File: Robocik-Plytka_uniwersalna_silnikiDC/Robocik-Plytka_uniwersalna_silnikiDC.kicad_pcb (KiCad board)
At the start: 2 copper layers, 49.6 x 66.8 mm, 67 parts, among them IC1 ACSL-6400-00TE, IC2 L6205D, J1 Conn_01x03, J2 Conn_01x02, J3 Conn_01x04, J4 Conn_01x02, J5 Conn_01x03, J6 Conn_01x02, Q1 BC847, Q2 BC847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

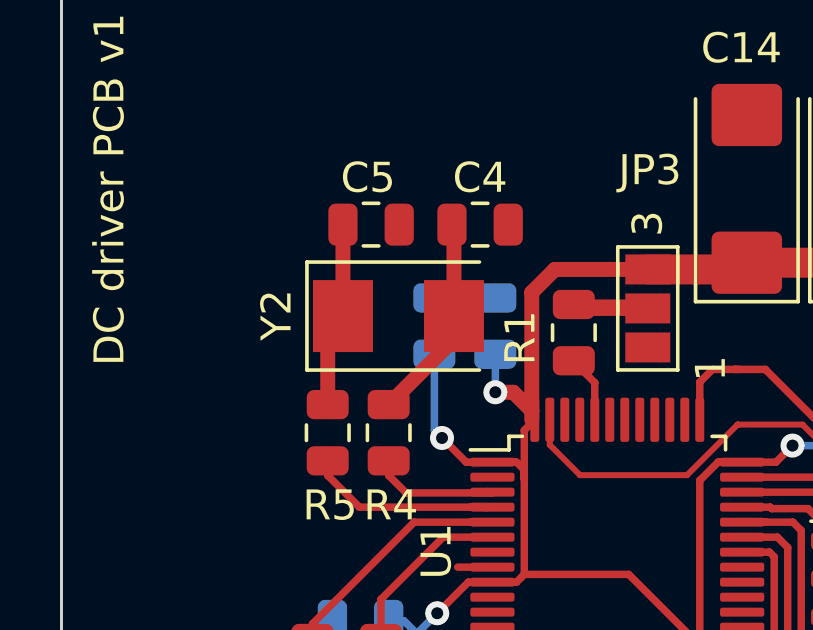
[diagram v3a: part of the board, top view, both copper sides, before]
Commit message: Fixed size of LSE crystal oscilator. Added 3D models for LSE and HSE oscilators.
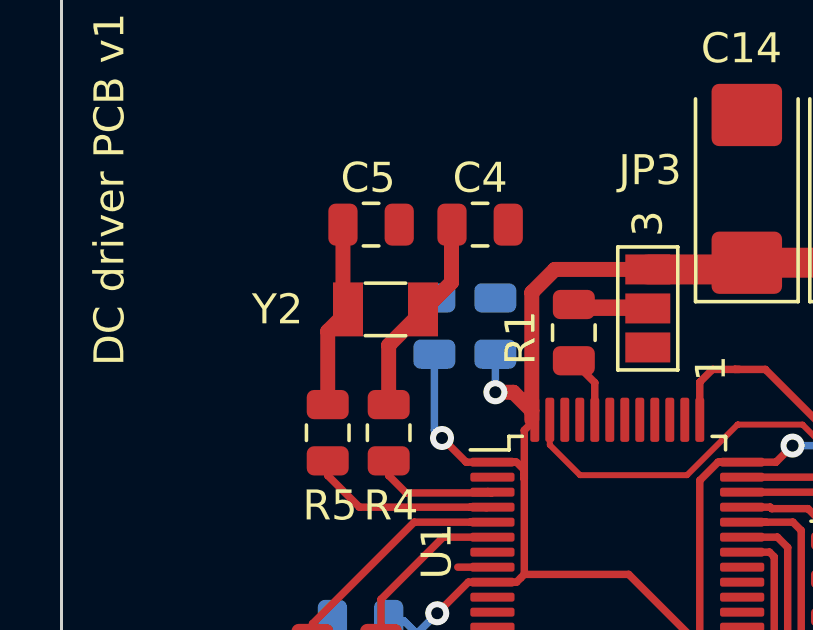
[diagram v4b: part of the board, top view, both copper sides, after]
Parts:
- Y2: footprint Crystal:Crystal_SMD_5032-2Pin_5.0x3.2mm -> Crystal:Crystal_SMD_3215-2Pin_3.2x1.5mm
- moved Y2 0.49 mm to (135.2, 81.6), turned to 180 degrees
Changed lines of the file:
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@@
     (thickness 1.6)
     (drawings 13)
-    (tracks 472)
+    (tracks 473)
     (zones 0)
     (modules 67)
@@
   )
   (setup
-    (last_trace_width 0.25)
+    (last_trace_width 0.5)
     (user_trace_width 0.2)
     (user_trace_width 0.5)
@@
     (add_net VddPWR)
   )
+  (module Crystal:Crystal_SMD_3215-2Pin_3.2x1.5mm (layer F.Cu)
+    (at 135.2 81.6 180)
+    (descr "SMD Crystal FC-135 https://support.epson.biz/td/api/doc_check.php?dl=brief_FC-135R_en.pdf")
+    (tags "SMD SMT Crystal")
+    (attr smd)
+    (fp_text reference Y2 (at 3.6 0 180) (layer F.SilkS)
+      (effects (font (size 1 1) (thickness 0.15)))
+    )
+    (fp_text value "LSE OSC" (at 0 2 180) (layer F.Fab)
+      (effects (font (size 1 1) (thickness 0.15)))
+    )
+    (fp_line (start 2 -1.15) (end 2 1.15) (layer F.CrtYd) (width 0.05))
+    (fp_line (start -2 -1.15) (end -2 1.15) (layer F.CrtYd) (width 0.05))
+    (fp_line (start -2 1.15) (end 2 1.15) (layer F.CrtYd) (width 0.05))
+    (fp_line (start -1.6 0.75) (end 1.6 0.75) (layer F.Fab) (width 0.1))
+    (fp_line (start -1.6 -0.75) (end 1.6 -0.75) (layer F.Fab) (width 0.1))
+    (fp_line (start 1.6 -0.75) (end 1.6 0.75) (layer F.Fab) (width 0.1))
+    (fp_line (start -0.675 -0.875) (end 0.675 -0.875) (layer F.SilkS) (width 0.12))
+    (fp_line (start -0.675 0.875) (end 0.675 0.875) (layer F.SilkS) (width 0.12))
+    (fp_line (start -1.6 -0.75) (end -1.6 0.75) (layer F.Fab) (width 0.1))
+    (fp_line (start -2 -1.15) (end 2 -1.15) (layer F.CrtYd) (width 0.05))
+    (fp_text user %R (at 0 -2 180) (layer F.Fab)
+      (effects (font (size 1 1) (thickness 0.15)))
+    )
+    (pad 2 smd rect (at -1.25 0 180) (size 1 1.8) (layers F.Cu F.Paste F.Mask)
+      (net 5 "Net-(C4-Pad2)"))
+    (pad 1 smd rect (at 1.25 0 180) (size 1 1.8) (layers F.Cu F.Paste F.Mask)
+      (net 6 "Net-(C5-Pad2)"))
+    (model ${KISYS3DMOD}/Crystal.3dshapes/Crystal_SMD_3215-2Pin_3.2x1.5mm.wrl
+      (at (xyz 0 0 0))
+      (scale (xyz 1 1 1))
+      (rotate (xyz 0 0 0))
+    )
+    (model "${KIPRJMOD}/3D models/Crystal_SMD-3,2x1,5.STEP"
+      (at (xyz 0 0 0))
+      (scale (xyz 1 1 1))
+      (rotate (xyz -90 0 90))
+    )
+  )
   (module Connector_JST:JST_PH_S3B-PH-K_1x03_P2.00mm_Horizontal (layer B.Cu)
     (at 167 101.1 270)
@@
   )
   (module Crystal:Crystal_SMD_5032-2Pin_5.0x3.2mm (layer F.Cu)
-    (at 135.632 81.822)
-    (descr "SMD Crystal SERIES SMD2520/2 http://www.icbase.com/File/PDF/HKC/HKC00061008.pdf, 5.0x3.2mm^2 package")
-    (tags "SMD SMT crystal")
-    (attr smd)
-    (fp_text reference Y2 (at -4.06 -0.034 90) (layer F.SilkS)
-      (effects (font (size 1 1) (thickness 0.15)))
-    )
-    (fp_text value "LSE OSC" (at 0 2.8) (layer F.Fab)
-      (effects (font (size 1 1) (thickness 0.15)))
-    )
-    (fp_circle (center 0 0) (end 0.093333 0) (layer F.Adhes) (width 0.186667))
-    (fp_circle (center 0 0) (end 0.213333 0) (layer F.Adhes) (width 0.133333))
-    (fp_circle (center 0 0) (end 0.333333 0) (layer F.Adhes) (width 0.133333))
-    (fp_circle (center 0 0) (end 0.4 0) (layer F.Adhes) (width 0.1))
-    (fp_line (start 3.1 -1.9) (end -3.1 -1.9) (layer F.CrtYd) (width 0.05))
-    (fp_line (start 3.1 1.9) (end 3.1 -1.9) (layer F.CrtYd) (width 0.05))
-    (fp_line (start -3.1 1.9) (end 3.1 1.9) (layer F.CrtYd) (width 0.05))
-    (fp_line (start -3.1 -1.9) (end -3.1 1.9) (layer F.CrtYd) (width 0.05))
-    (fp_line (start -3.05 1.8) (end 2.7 1.8) (layer F.SilkS) (width 0.12))
-    (fp_line (start -3.05 -1.8) (end -3.05 1.8) (layer F.SilkS) (width 0.12))
-    (fp_line (start 2.7 -1.8) (end -3.05 -1.8) (layer F.SilkS) (width 0.12))
-    (fp_line (start -2.5 0.6) (end -1.5 1.6) (layer F.Fab) (width 0.1))
-    (fp_line (start -2.5 -1.4) (end -2.3 -1.6) (layer F.Fab) (width 0.1))
-    (fp_line (start -2.5 1.4) (end -2.5 -1.4) (layer F.Fab) (width 0.1))
-    (fp_line (start -2.3 1.6) (end -2.5 1.4) (layer F.Fab) (width 0.1))
-    (fp_line (start 2.3 1.6) (end -2.3 1.6) (layer F.Fab) (width 0.1))
-    (fp_line (start 2.5 1.4) (end 2.3 1.6) (layer F.Fab) (width 0.1))
-    (fp_line (start 2.5 -1.4) (end 2.5 1.4) (layer F.Fab) (width 0.1))
-    (fp_line (start 2.3 -1.6) (end 2.5 -1.4) (layer F.Fab) (width 0.1))
-    (fp_line (start -2.3 -1.6) (end 2.3 -1.6) (layer F.Fab) (width 0.1))
-    (fp_text user %R (at 0 0) (layer F.Fab)
-      (effects (font (size 1 1) (thickness 0.15)))
-    )
-    (pad 2 smd rect (at 1.85 0) (size 2 2.4) (layers F.Cu F.Paste F.Mask)
-      (net 5 "Net-(C4-Pad2)"))
-    (pad 1 smd rect (at -1.85 0) (size 2 2.4) (layers F.Cu F.Paste F.Mask)
-      (net 6 "Net-(C5-Pad2)"))
-    (model ${KISYS3DMOD}/Crystal.3dshapes/Crystal_SMD_5032-2Pin_5.0x3.2mm.wrl
-      (at (xyz 0 0 0))
-      (scale (xyz 1 1 1))
-      (rotate (xyz 0 0 0))
-    )
-  )
-  (module Crystal:Crystal_SMD_5032-2Pin_5.0x3.2mm (layer F.Cu)
     (at 134.87 97.316 180)
     (descr "SMD Crystal SERIES SMD2520/2 http://www.icbase.com/File/PDF/HKC/HKC00061008.pdf, 5.0x3.2mm^2 package")
@@
       (rotate (xyz 0 0 0))
     )
+    (model "${KIPRJMOD}/3D models/Crystal_SMD-5x3,2.STEP"
+      (at (xyz 0 0 0))
+      (scale (xyz 1 1 1))
+      (rotate (xyz 0 0 0))
+    )
   )
   (module Package_TO_SOT_SMD:SOT-223-3_TabPin2 (layer F.Cu)
@@
   (segment (start 135.3845 98.6515) (end 136.72 97.316) (width 0.5) (layer F.Cu) (net 4))
   (segment (start 135.3845 100.364) (end 135.3845 98.6515) (width 0.5) (layer F.Cu) (net 4))
-  (segment (start 137.482 82.597) (end 135.306 84.773) (width 0.5) (layer F.Cu) (net 5))
-  (segment (start 137.482 81.822) (end 137.482 82.597) (width 0.5) (layer F.Cu) (net 5))
   (segment (start 137.482 78.8395) (end 137.4165 78.774) (width 0.5) (layer F.Cu) (net 5))
-  (segment (start 137.482 81.822) (end 137.482 78.8395) (width 0.5) (layer F.Cu) (net 5))
+  (segment (start 135.306 84.773) (end 135.306 82.794) (width 0.5) (layer F.Cu) (net 5))
+  (segment (start 135.306 82.794) (end 136.5 81.6) (width 0.5) (layer F.Cu) (net 5))
+  (segment (start 136.5 81.6) (end 137.4 80.7) (width 0.5) (layer F.Cu) (net 5))
+  (segment (start 137.4 80.7) (end 137.4 78.8) (width 0.5) (layer F.Cu) (net 5))
   (segment (start 133.274 82.33) (end 133.782 81.822) (width 0.5) (layer F.Cu) (net 6))
   (segment (start 133.274 84.773) (end 133.274 82.33) (width 0.5) (layer F.Cu) (net 6))

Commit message: fixed gnda layer
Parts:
- C16, C17: value 5.6nF -> 10nF
- C2, C3: value 100nF -> 27pF
- C4, C5: value 100nF -> 8.2pF
- R19, R20: value 100k -> 56k
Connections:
- IC1 pad 9: Net-(IC1-Pad9) -> GNDA

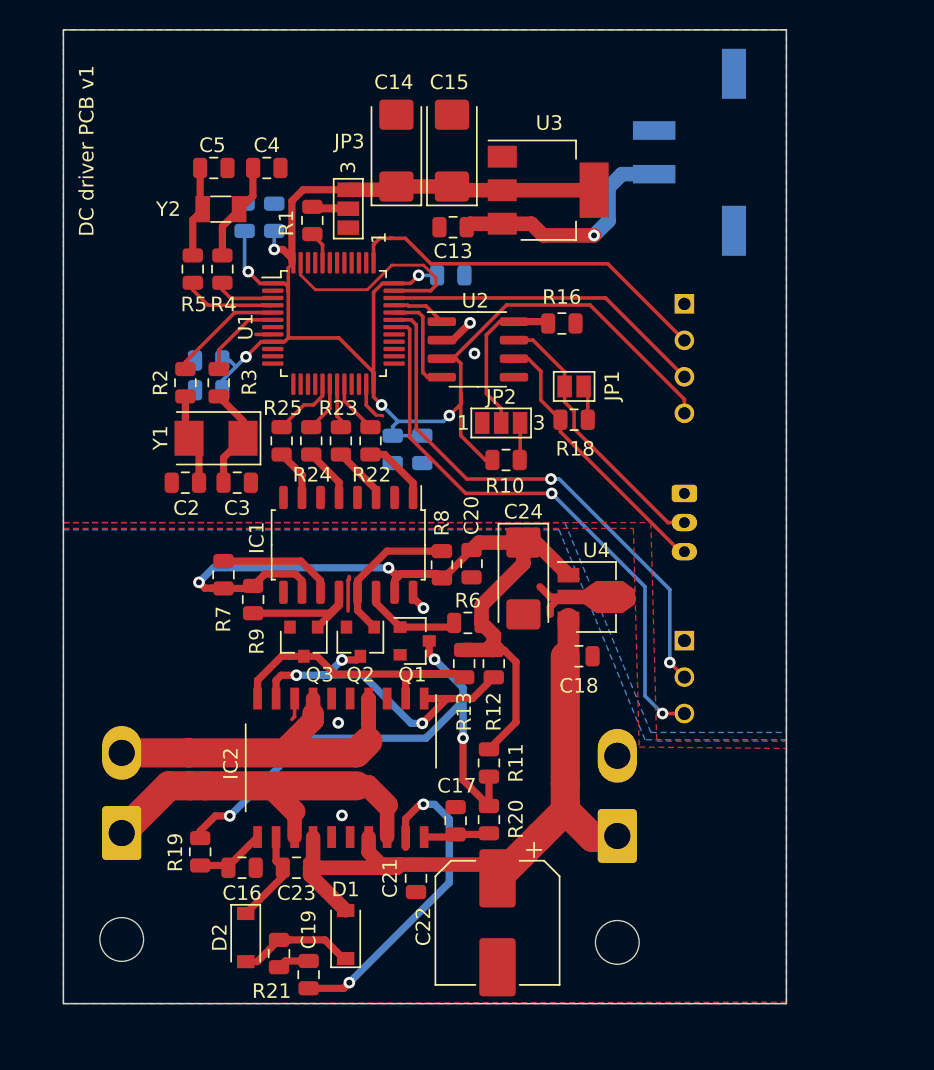
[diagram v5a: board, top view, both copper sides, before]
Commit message: Reduced size of a board, added mounting holes and description of max current and voltage
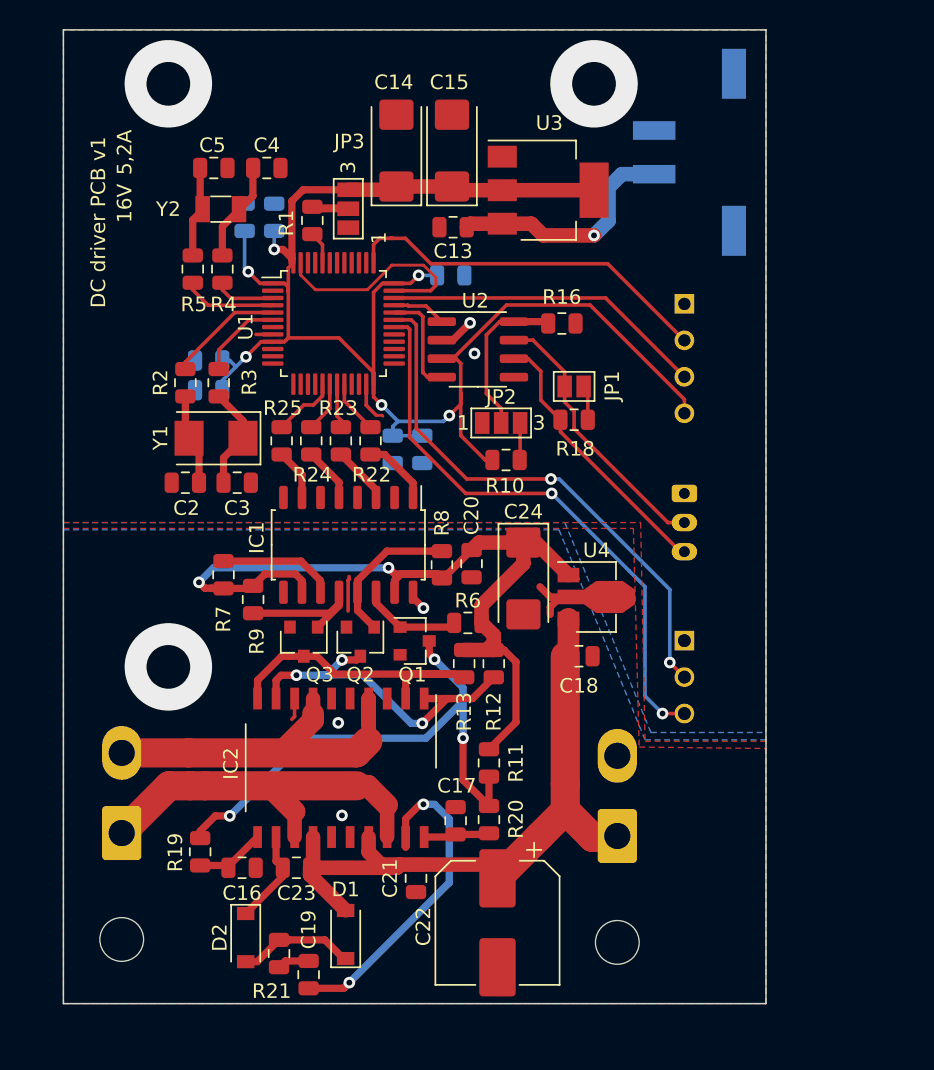
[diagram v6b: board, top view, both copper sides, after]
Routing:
- net (no net): vias 0 -> 3
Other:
- board size 49.6 x 66.8 mm -> 48.2 x 66.8 mm
- board text added: "16V"
- board text added: "5,2A"
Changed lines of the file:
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@@
   (general
     (thickness 1.6)
-    (drawings 13)
-    (tracks 473)
+    (drawings 15)
+    (tracks 476)
     (zones 0)
     (modules 67)
@@
     (via_min_drill 0.3)
     (user_via 2 1)
+    (user_via 6 3)
     (uvia_size 0.3)
     (uvia_drill 0.1)
@@
     )
   )
-  (gr_text "DC driver PCB v1" (at 126 77.6 90) (layer F.SilkS)
+  (gr_text 16V (at 128.6 81.2 90) (layer F.SilkS)
+    (effects (font (size 1 1) (thickness 0.15)))
+  )
+  (gr_text 5,2A (at 128.6 77.7 90) (layer F.SilkS)
+    (effects (font (size 1 1) (thickness 0.15)))
+  )
+  (gr_text "DC driver PCB v1" (at 126.8 82.5 90) (layer F.SilkS)
     (effects (font (size 1 1) (thickness 0.15)))
   )
@@
   )
   (dimension 66.8 (width 0.15) (layer Dwgs.User)
-    (gr_text "66,800 mm" (at 186.7 102.7 270) (layer Dwgs.User)
+    (gr_text "66,800 mm" (at 185.3 102.7 270) (layer Dwgs.User)
       (effects (font (size 1 1) (thickness 0.15)))
     )
-    (feature1 (pts (xy 174 136.1) (xy 185.986421 136.1)))
-    (feature2 (pts (xy 174 69.3) (xy 185.986421 69.3)))
-    (crossbar (pts (xy 185.4 69.3) (xy 185.4 136.1)))
-    (arrow1a (pts (xy 185.4 136.1) (xy 184.813579 134.973496)))
-    (arrow1b (pts (xy 185.4 136.1) (xy 185.986421 134.973496)))
-    (arrow2a (pts (xy 185.4 69.3) (xy 184.813579 70.426504)))
-    (arrow2b (pts (xy 185.4 69.3) (xy 185.986421 70.426504)))
+    (feature1 (pts (xy 172.6 136.1) (xy 184.586421 136.1)))
+    (feature2 (pts (xy 172.6 69.3) (xy 184.586421 69.3)))
+    (crossbar (pts (xy 184 69.3) (xy 184 136.1)))
+    (arrow1a (pts (xy 184 136.1) (xy 183.413579 134.973496)))
+    (arrow1b (pts (xy 184 136.1) (xy 184.586421 134.973496)))
+    (arrow2a (pts (xy 184 69.3) (xy 183.413579 70.426504)))
+    (arrow2b (pts (xy 184 69.3) (xy 184.586421 70.426504)))
   )
-  (dimension 49.6 (width 0.15) (layer Dwgs.User)
-    (gr_text "49,600 mm" (at 149.2 61.7) (layer Dwgs.User)
+  (dimension 48.2 (width 0.15) (layer Dwgs.User)
+    (gr_text "48,200 mm" (at 148.5 61.7) (layer Dwgs.User)
       (effects (font (size 1 1) (thickness 0.15)))
     )
-    (feature1 (pts (xy 174 69.3) (xy 174 62.413579)))
+    (feature1 (pts (xy 172.6 69.3) (xy 172.6 62.413579)))
     (feature2 (pts (xy 124.4 69.3) (xy 124.4 62.413579)))
-    (crossbar (pts (xy 124.4 63) (xy 174 63)))
-    (arrow1a (pts (xy 174 63) (xy 172.873496 63.586421)))
-    (arrow1b (pts (xy 174 63) (xy 172.873496 62.413579)))
+    (crossbar (pts (xy 124.4 63) (xy 172.6 63)))
+    (arrow1a (pts (xy 172.6 63) (xy 171.473496 63.586421)))
+    (arrow1b (pts (xy 172.6 63) (xy 171.473496 62.413579)))
     (arrow2a (pts (xy 124.4 63) (xy 125.526504 63.586421)))
     (arrow2b (pts (xy 124.4 63) (xy 125.526504 62.413579)))
   )
-  (gr_line (start 174 136.1) (end 174 69.3) (layer Edge.Cuts) (width 0.1))
-  (gr_line (start 124.4 136.1) (end 174 136.1) (layer Edge.Cuts) (width 0.1))
+  (gr_line (start 172.6 136.1) (end 172.6 69.3) (layer Edge.Cuts) (width 0.1))
+  (gr_line (start 124.4 136.1) (end 172.6 136.1) (layer Edge.Cuts) (width 0.1))
   (gr_line (start 124.4 69.3) (end 124.4 136.1) (layer Edge.Cuts) (width 0.1))
-  (gr_line (start 174 69.3) (end 124.4 69.3) (layer Edge.Cuts) (width 0.1))
+  (gr_line (start 172.6 69.3) (end 124.4 69.3) (layer Edge.Cuts) (width 0.1))
   (segment (start 145.176 95.051002) (end 145.866488 95.74149) (width 0.25) (layer F.Cu) (net 1))
   (segment (start 145.176 93.6045) (end 145.176 95.051002) (width 0.25) (layer F.Cu) (net 1))
@@
   (segment (start 149.592 87.192) (end 149.960946 86.823054) (width 0.25) (layer F.Cu) (net 1))
   (via (at 152.6 91.5) (size 0.8) (drill 0.4) (layers F.Cu B.Cu) (net 1))
+  (via (at 131.6 73) (size 6) (drill 3) (layers F.Cu B.Cu) (net 0))
+  (via (at 160.8 73) (size 6) (drill 3) (layers F.Cu B.Cu) (net 0))
+  (via (at 131.6 113) (size 6) (drill 3) (layers F.Cu B.Cu) (net 0))
   (segment (start 147.0885 86.692) (end 148.216 86.692) (width 0.25) (layer F.Cu) (net 2))
   (segment (start 148.216 86.692) (end 148.768 86.14) (width 0.25) (layer F.Cu) (net 2))
@@
     (polygon
       (pts
-        (xy 124.4 69.3) (xy 124.4 103.1) (xy 164.7 103.1) (xy 165.1 118.1) (xy 174 118.1)
-        (xy 174 69.3)
+        (xy 124.4 69.3) (xy 124.4 103.1) (xy 164 103.1) (xy 164.3 118.1) (xy 172.6 118.1)
+        (xy 172.6 69.3)
       )
     )
@@
     (connect_pads (clearance 0.25))
     (min_thickness 0.254)
-    (fill yes (arc_segments 32) (thermal_gap 0.508) (thermal_bridge_width 0.508))
+    (fill yes (arc_segments 32) (thermal_gap 0.508) (thermal_bridge_width 1))
     (polygon
       (pts
-        (xy 124.4 103.5) (xy 163.5 103.5) (xy 163.9 118.5) (xy 174 118.6) (xy 174 136)
+        (xy 124.4 103.5) (xy 163.5 103.5) (xy 163.9 118.5) (xy 172.6 118.6) (xy 172.6 136.1)
         (xy 124.4 136.1)
       )
@@
     (connect_pads (clearance 0.25))
     (min_thickness 0.254)
-    (fill yes (arc_segments 32) (thermal_gap 0.508) (thermal_bridge_width 0.508))
+    (fill yes (arc_segments 32) (thermal_gap 0.508) (thermal_bridge_width 1))
     (polygon
       (pts
-        (xy 124.4 69.3) (xy 124.4 103.1) (xy 158.8 103.1) (xy 164.7 117.5) (xy 174 117.5)
-        (xy 174 69.3)
+        (xy 124.4 69.3) (xy 124.4 103.1) (xy 158.8 103.1) (xy 164.7 117.5) (xy 172.6 117.5)
+        (xy 172.6 69.3)
       )
     )
@@
     (connect_pads (clearance 0.25))
     (min_thickness 0.254)
-    (fill yes (arc_segments 32) (thermal_gap 0.508) (thermal_bridge_width 0.508))
+    (fill yes (arc_segments 32) (thermal_gap 0.508) (thermal_bridge_width 1))
     (polygon
       (pts
-        (xy 124.4 103.6) (xy 124.4 136.1) (xy 174 136.1) (xy 174 118) (xy 164.3 118)
+        (xy 124.4 103.6) (xy 124.4 136.1) (xy 172.6 136.1) (xy 172.6 118) (xy 164.3 118)
         (xy 158.4 103.6)
       )
